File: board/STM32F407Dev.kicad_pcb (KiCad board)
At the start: 2 copper layers, 60 x 36 mm, 61 parts, among them J1 USB_C_Receptacle_USB2.0_16P, J2 Conn_01x08_MountingPin, J3 Conn_02x19_Odd_Even, J4 Conn_02x19_Odd_Even, J5 Conn_01x04, Q1 AO3401A, SW1 SW_Push, SW2 SW_Push, SW3 SW_Push, SW4 SW_Push, U1 STM32F407VGTx, U2 W25N01GVZE, U3 ME6211C33M5, Y1 24MHz, Y2 32.768kHz

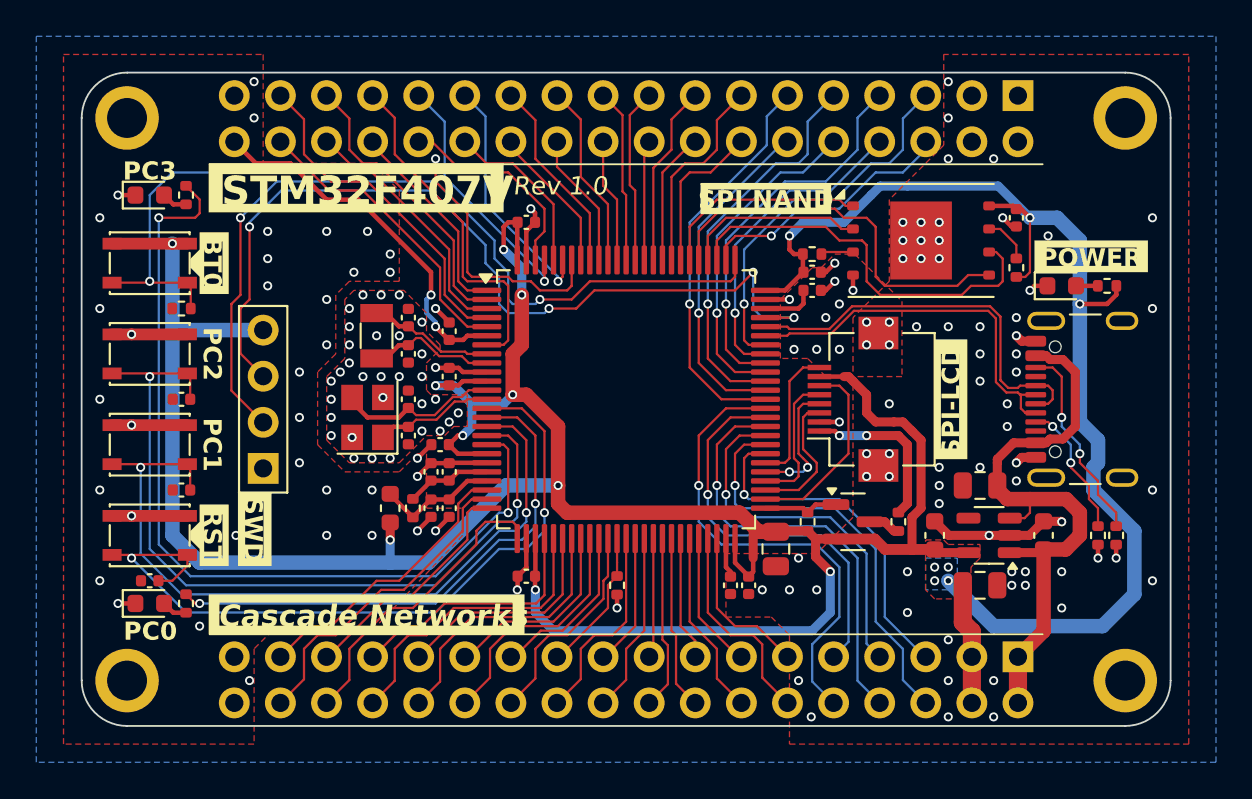
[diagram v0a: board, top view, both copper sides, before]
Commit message: Update STM32F407 file, delete backup and lock
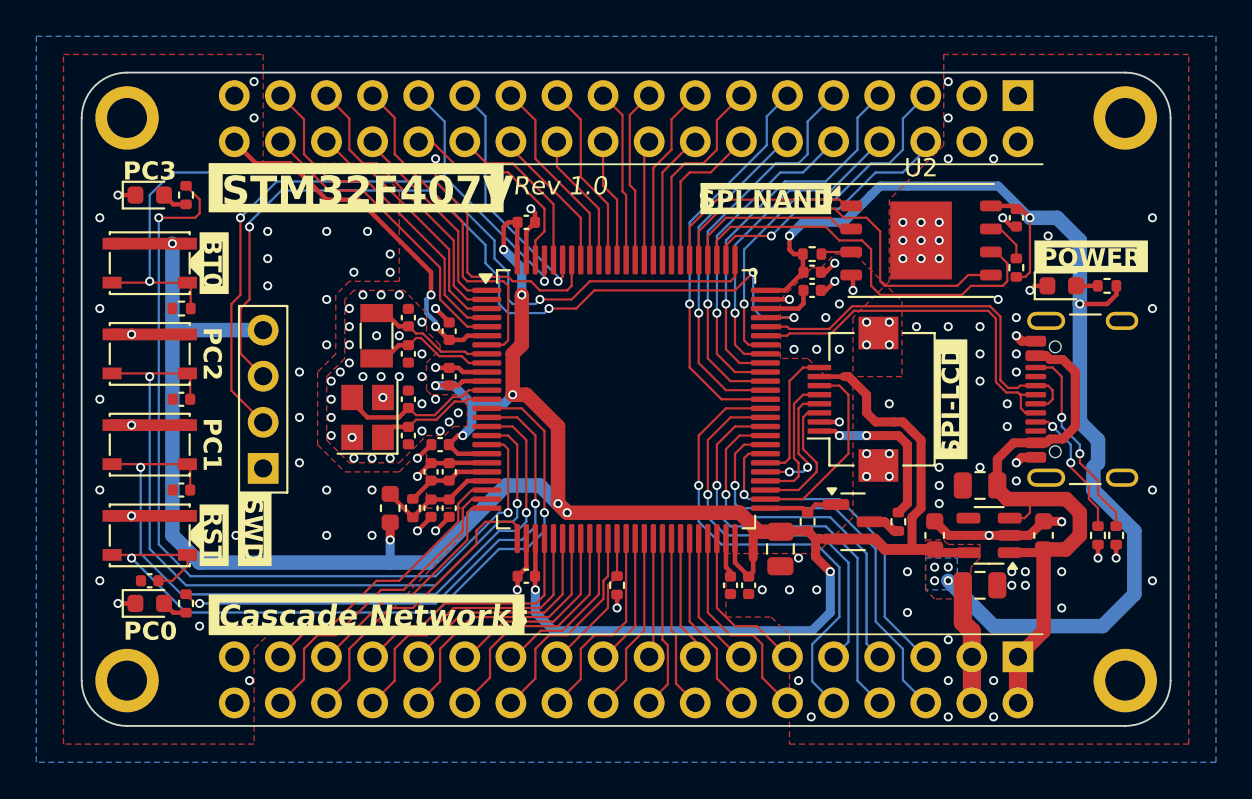
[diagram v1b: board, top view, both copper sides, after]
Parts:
- C23: value 22uF -> 10uF
- U2: footprint Package_SON:WSON-8-1EP_8x6mm_P1.27mm_EP3.4x4.3mm -> Cascade_SON:WSON-8-1EP_8x6mm_P1.27mm_EP3.4x4.3mm_WidePin
- moved C26 0.25 mm to (158.5, 108.2)
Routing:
- net +3.3V: track 225.5 -> 226.6 mm, vias 17 -> 18
- net GND: vias 151 -> 152
